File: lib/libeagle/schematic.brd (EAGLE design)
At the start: 100 x 80 mm, 1 part, among them IC1 75162P

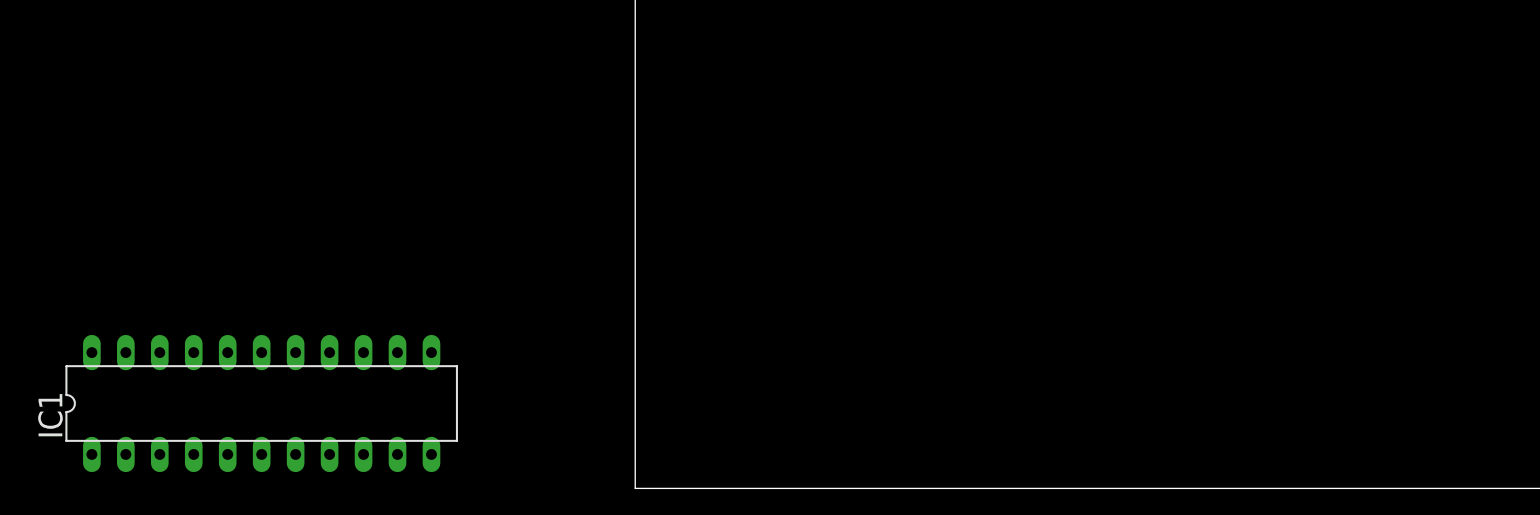
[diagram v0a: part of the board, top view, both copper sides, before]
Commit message: Primary parser done.
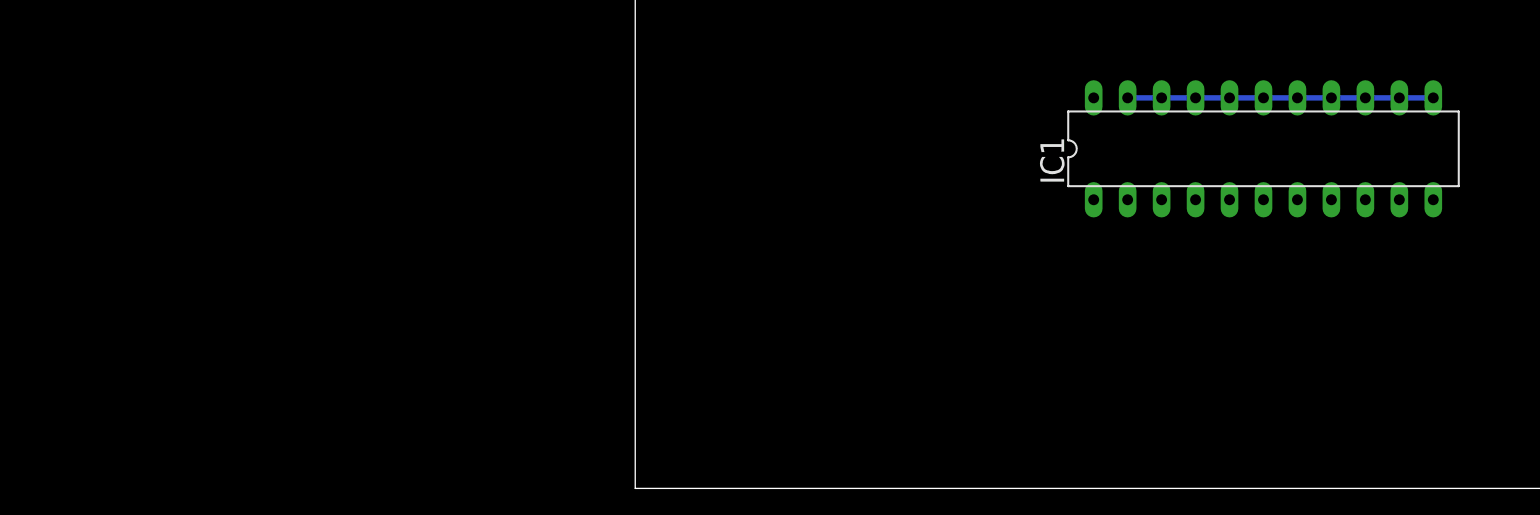
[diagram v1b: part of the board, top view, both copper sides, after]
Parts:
- moved IC1 77.3 mm to (47.0, 25.4)
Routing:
- net N$2: track 0.00 -> 22.9 mm
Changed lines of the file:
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@@
 </autorouter>
 <elements>
-<element name="IC1" library="751xx" package="DIL22-3" value="75162P" x="-27.94" y="6.35"/>
+<element name="IC1" library="751xx" package="DIL22-3" value="75162P" x="46.99" y="25.4"/>
 </elements>
 <signals>
@@
 <contactref element="IC1" pad="21"/>
 <contactref element="IC1" pad="12"/>
-<wire x1="-15.24" y1="10.16" x2="-38.1" y2="10.16" width="0" layer="19" extent="1-1"/>
+<wire x1="36.83" y1="29.21" x2="59.69" y2="29.21" width="0.4064" layer="16"/>
 </signal>
 </signals>
